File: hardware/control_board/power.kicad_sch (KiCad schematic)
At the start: 1 part, among them U1 STUSB4500QTR

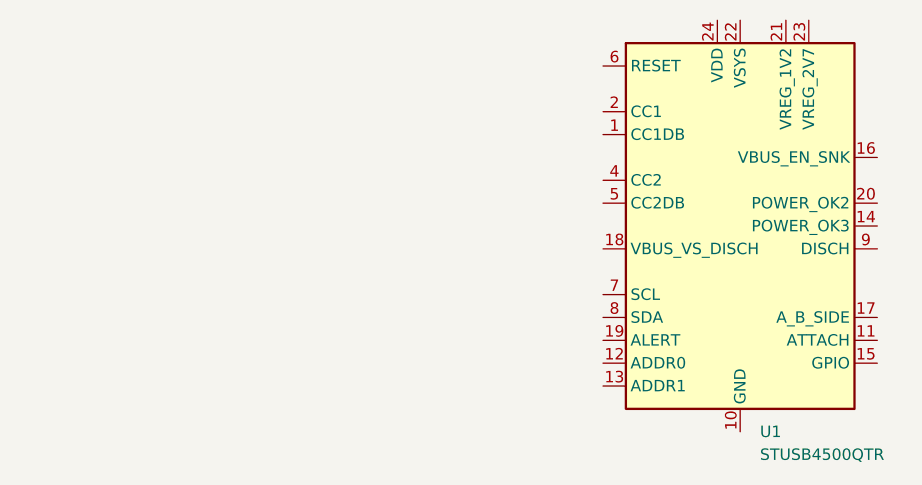
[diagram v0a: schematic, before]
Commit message: added symbols and footprints
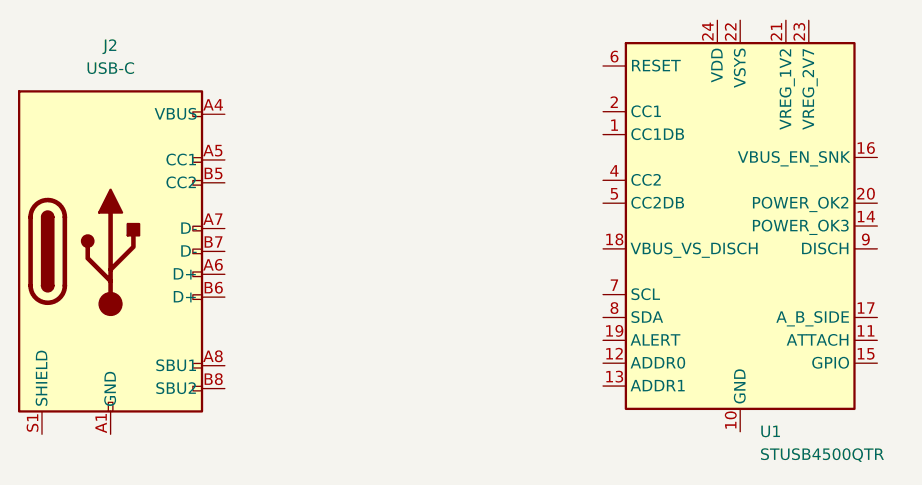
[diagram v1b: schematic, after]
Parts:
- added J2: USB-C, Library:USB-C, symbol Library:USB-C
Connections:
- new net: J2.A1 (GND), J2.A12 (GND), J2.B1 (GND), J2.B12 (GND)
- new net: J2.A4 (VBUS), J2.A9 (VBUS), J2.B4 (VBUS), J2.B9 (VBUS)
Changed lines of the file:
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@@
 	(paper "A4")
+	(symbol
+		(lib_id "Library:USB-C")
+		(at 60.96 83.82 0)
+		(unit 1)
+		(exclude_from_sim no)
+		(in_bom yes)
+		(on_board yes)
+		(dnp no)
+		(fields_autoplaced yes)
+		(property "Reference" "J2"
+			(at 60.96 60.96 0)
+			(effects
+				(font
+					(size 1.27 1.27)
+				)
+			)
+		)
+		(property "Value" "USB-C"
+			(at 60.96 63.5 0)
+			(effects
+				(font
+					(size 1.27 1.27)
+				)
+			)
+		)
+		(property "Footprint" "Library:USB-C"
+			(at 60.452 112.776 0)
+			(effects
+				(font
+					(size 1.27 1.27)
+				)
+				(hide yes)
+			)
+		)
+		(property "Datasheet" ""
+			(at 60.452 112.776 0)
+			(effects
+				(font
+					(size 1.27 1.27)
+				)
+				(hide yes)
+			)
+		)
+		(property "Description" "USB-C Jack"
+			(at 60.96 115.062 0)
+			(effects
+				(font
+					(size 1.27 1.27)
+				)
+				(hide yes)
+			)
+		)
+		(pin "A7"
+		)
+		(pin "B12"
+		)
+		(pin "S1"
+		)
+		(pin "A9"
+		)
+		(pin "B4"
+		)
+		(pin "A8"
+		)
+		(pin "B8"
+		)
+		(pin "B1"
+		)
+		(pin "A12"
+		)
+		(pin "A1"
+		)
+		(pin "B5"
+		)
+		(pin "B7"
+		)
+		(pin "A4"
+		)
+		(pin "B9"
+		)
+		(pin "A6"
+		)
+		(pin "B6"
+		)
+		(pin "A5"
+		)
+		(instances
+			(project "control_board"
+				(path "/acca031a-6f31-41bd-bf7c-a4abb4bf7051/c43f2e3f-578b-42a9-b824-c6330d141f17"
+					(reference "J2")
+					(unit 1)
+				)
+			)
+		)
+	)
 	(symbol
 		(lib_id "Interface_USB:STUSB4500QTR")
